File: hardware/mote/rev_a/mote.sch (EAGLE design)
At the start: 57 parts, among them Q1 CSD22206W, Q2 CSD75207W15, Q3 CSD75207W15, Q4 CSD13303W1015, Q5 CSD22206W, U1 NRF52840, U3 MAX17222, U4 TPS3839G25DBZ, U5 AB1815-T3, X1 7V-32.000MAHV-T, X2 ABS07-32.768KHZ-7-T

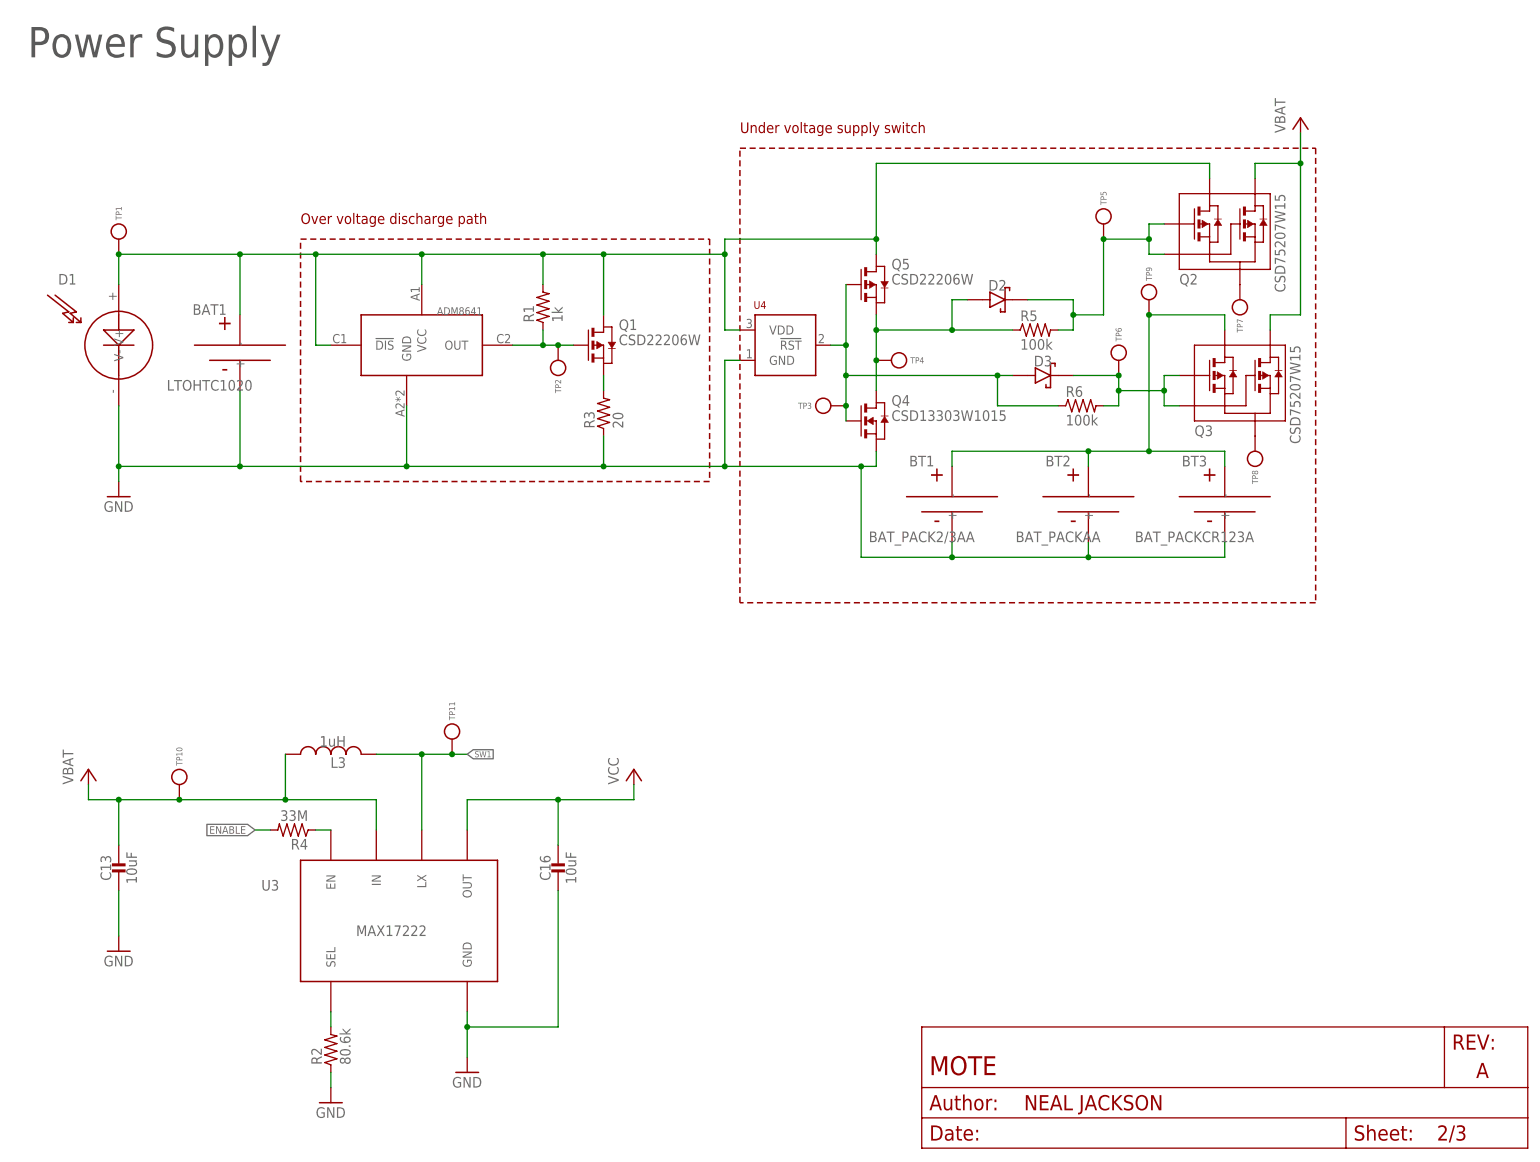
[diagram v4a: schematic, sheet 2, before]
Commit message: Schematized sensors and cleaned up
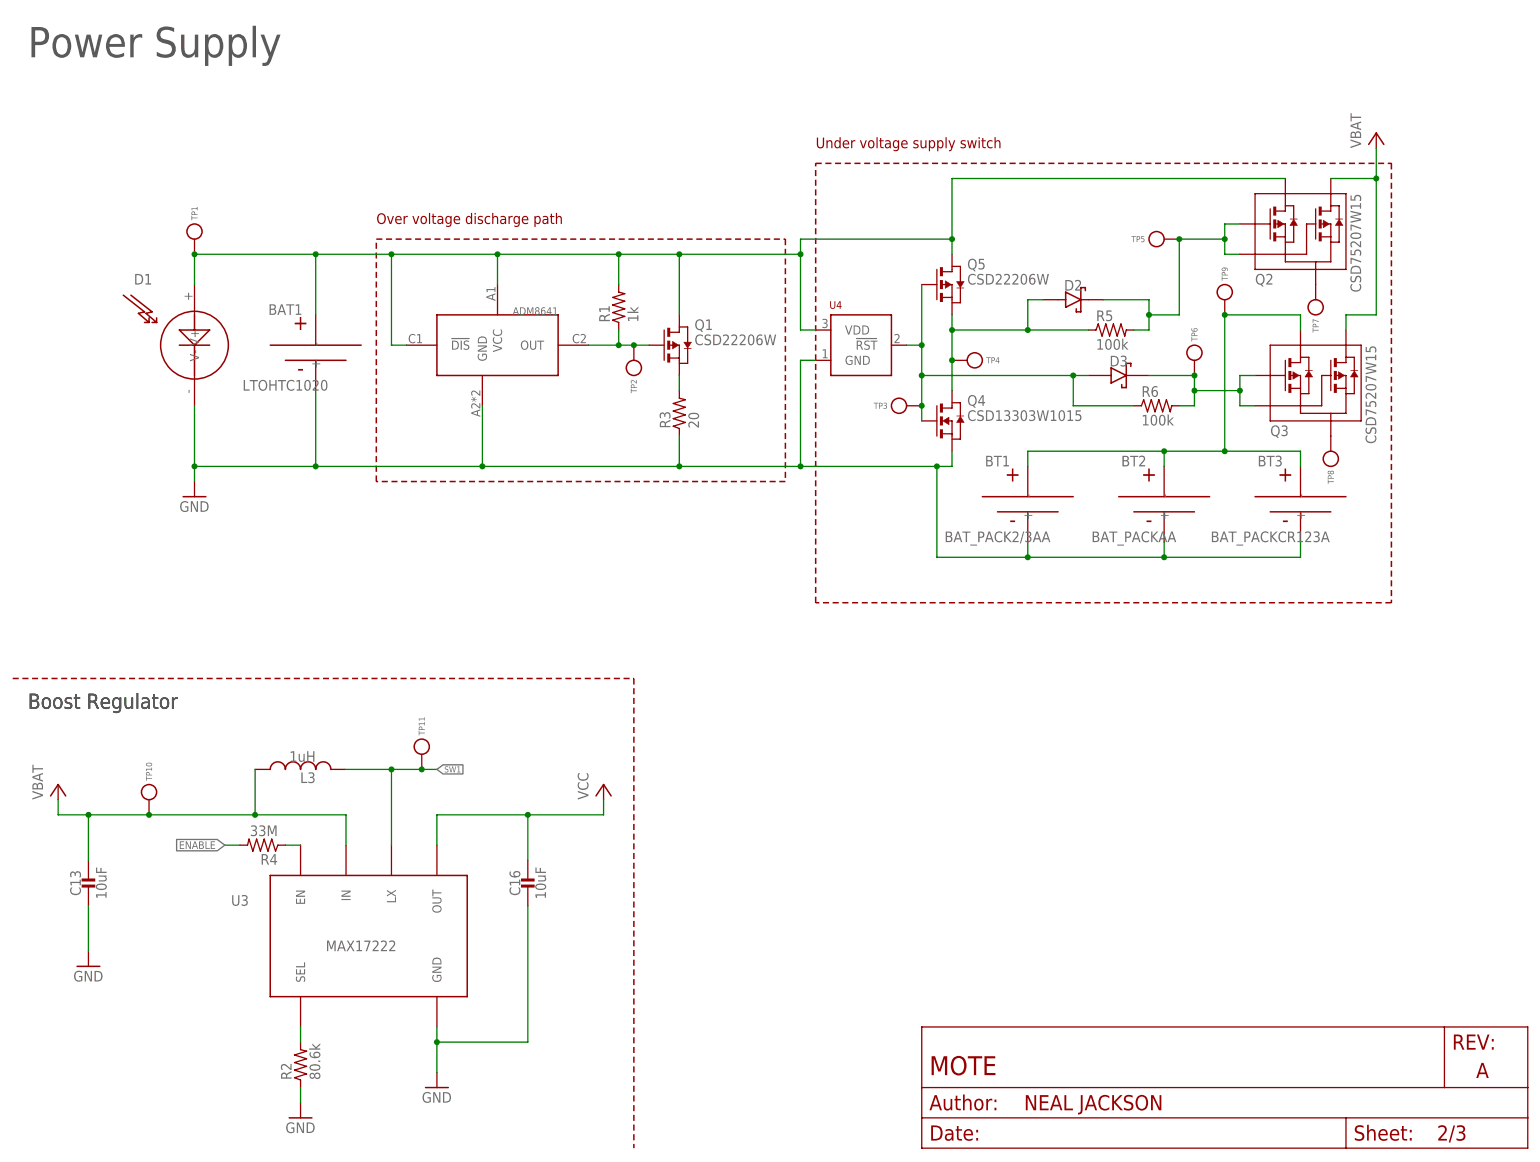
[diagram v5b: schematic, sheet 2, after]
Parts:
- removed X2: ABS07-32.768KHZ-7-T, crystals:ABS07-32.768KHZ-7-T
- added C19, C20: 0.1uF, passives:CAPACITOR0402_CAP
- added C21, C25: 1.0uF, passives:CAPACITOR0402_CAP
- added C22: 47pF, passives:CAPACITOR0402_CAP
- added C23, C24: DNP, passives:CAPACITOR0402_CAP
- added R7, R8: 10k, passives:RESISTOR0402_RES
- added U10: MS5637-02BA03, chips:MS5637-02BA03
- added U6: ISL29125, chips:ISL29125
- added U7: MAX44009, chips:MAX44009
- added U8: LIS2DW12, chips:LIS2DW12
- added U9: AB1815-T3, chips:AB1815-T3
- added X3: ABS07-32.768KHZ-7-T, crystals:ABS07-32.768KHZ-7-T
- C10: value 1uF -> 1.0uF; DIGIKEY (none) -> 490-7195-1-ND
- C17: value DNP -> 10uF; device passives:CAPACITOR0402_CAP -> passives:CAPACITOR0603_CAP; DIGIKEY (none) -> 490-3896-2-ND
- C18: value DNP -> 0.1uF; DIGIKEY (none) -> 490-6328-1-ND
- C9: value 47pF -> 0.1uF; DIGIKEY (none) -> 490-6328-1-ND
- D2, D3: value DIODE_SCHOTTKYSOD323 -> DIODE_SCHOTTKYMBR0520LT1G; device passives:DIODE_SCHOTTKYSOD323 -> passives:DIODE_SCHOTTKYMBR0520LT1G; DIGIKEY (none) -> 1727-7328-1-ND; MANUFACTURER (none) -> Nexperia; MPN (none) -> BAT54GWJ
- R1: DIGIKEY (none) -> 311-1.0KJRCT-ND
- R3: DIGIKEY (none) -> 311-20JRCT-ND
- R5, R6: DIGIKEY (none) -> 311-100KLRCT-ND
- U5: value AB1815-T3 -> SI7021-A20-GM1; device chips:AB1815-T3 -> chips:SI7021-A20-GM1
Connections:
- removed net N$19: C17.1, U5.XI, X2.1
- removed net N$20: C18.1, U5.XO, X2.2
- removed net N$21: C9.1, U5.AF
- new net !CLR_INT: U6.!INT
- new net !LGHT_INT: U7.!INT
- new net ACL_CS: U8.CS
- new net ACL_INT1: U8.INT1
- new net ACL_INT2: U8.INT2
- new net N$25: C22.1, U9.AF
- new net N$26: C23.1, U9.XI, X3.1
- new net N$27: C24.1, U9.XO, X3.2
- new net SCK: U8.SCL/SPC, U9.SCL
- new net SDA: R8.1, U10.SDA, U5.SDA, U6.SDA, U7.SDA
- net !RTC_EXTR: now also U9.!EXTR; no longer U5.!EXTR
- net !RTC_IRQ1: now also U9.FOUT/!IRQ1; no longer U5.FOUT/!IRQ1
- net !RTC_IRQ2: now also U9.!IRQ2; no longer U5.!IRQ2
- net !RTC_RESET: now also U9.!RST; no longer U5.!RST
- net CLKOUT: now also U9.CLKOUT/!IRQ3; no longer U5.CLKOUT/!IRQ3
- net CS_RTC: now also U9.!CS; no longer U5.!CS
- net GND: now also C19.2, C20.2, C21.2, C22.2, C23.2, C24.2, C25.2, U10.GND, U5.GND, U6.GND, U7.A0, U7.GND, U8.GND, U9.VSS; no longer U5.VSS
- net MISO: now also U8.MISO/SDA, U9.SDO; no longer U5.SDO
- net MOSI: now also U8.MOSI/SA0, U9.SDI; no longer U5.SDI
- net SCL: now also R7.1, U10.SCL, U6.SCL, U7.SCL
- net VCC: now also C17.1, C18.1, C19.1, C20.1, C21.1, C25.1, C9.1, R7.2, R8.2, U10.VDD, U6.VDD, U7.VCC, U8.VCC, U8.VDD_IO, U9.VCC
- net WDI: now also U9.WDI; no longer U5.WDI
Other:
- note added: "Accelerometer"
- note added: "Ambient Light"
- note added: "Boost Regulator"
- note added: "Humidity"
- note added: "Light Color"
- note added: "Pressure"
- note added: "RTC"
- note added: "Sensors"
- note added: "Temperature"
- moved on the sheet: A1, BAT1, BT1, BT2, BT3, C10, C13, C16, C17, C18, C9, D1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

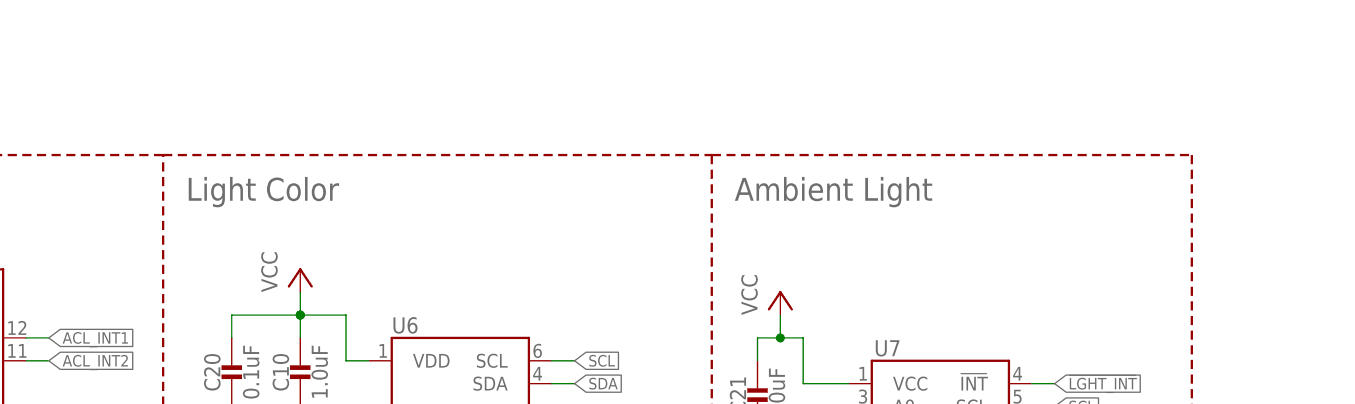
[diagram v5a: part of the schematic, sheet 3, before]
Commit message: add light subdivision
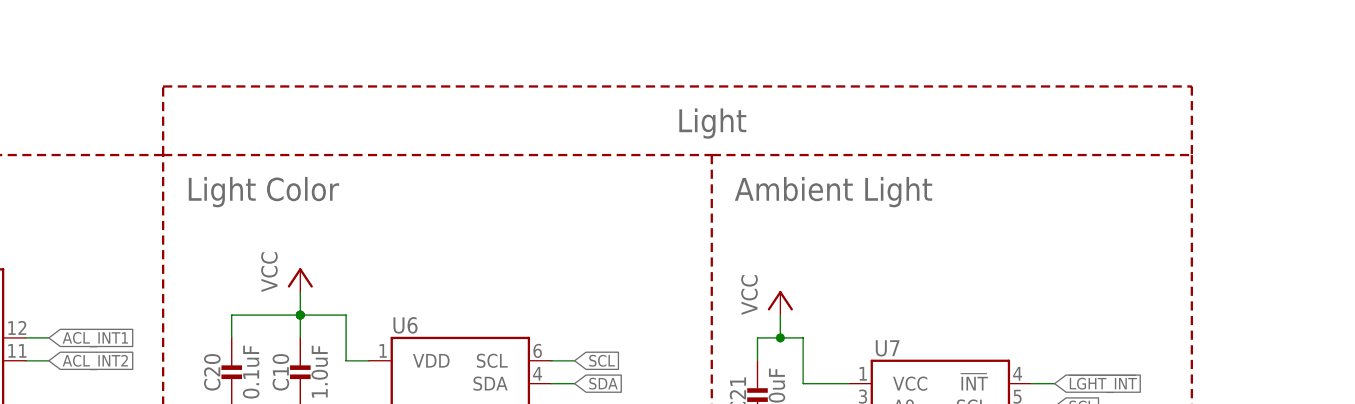
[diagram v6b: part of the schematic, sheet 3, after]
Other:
- note added: "Light"
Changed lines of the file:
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@@
 <wire x1="53.34" y1="121.92" x2="104.14" y2="121.92" width="0.254" layer="94" style="shortdash"/>
 <wire x1="53.34" y1="121.92" x2="0" y2="121.92" width="0.254" layer="94" style="shortdash"/>
+<text x="142.24" y="177.8" size="2.54" layer="95" align="bottom-center">Light</text>
+<wire x1="81.28" y1="175.26" x2="81.28" y2="182.88" width="0.254" layer="94" style="shortdash"/>
+<wire x1="81.28" y1="182.88" x2="195.58" y2="182.88" width="0.254" layer="94" style="shortdash"/>
+<wire x1="195.58" y1="182.88" x2="195.58" y2="175.26" width="0.254" layer="94" style="shortdash"/>
 </plain>
 <instances>

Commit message: made changes from josh
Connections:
- removed net !RTC_RESET: U9.!RST
- removed net N$22: BT1.+, BT2.+, BT3.+, Q3.D1, TP9.TESTPOINT
- new net !RST: U1.P0.18/RST, U9.!RST
- new net VSW: C13.1, L3.1, Q2.D2, Q3.D2, TP10.TESTPOINT, U3.IN
- net N$1: now also Q5.D; no longer Q5.S
- net N$24: now also Q5.S; no longer Q5.D
- net VBAT: now also BT1.+, BT2.+, BT3.+, C25.1, Q3.D1, TP9.TESTPOINT, U9.VCC; no longer C13.1, L3.1, Q2.D2, Q3.D2, TP10.TESTPOINT, U3.IN
- net VCC: no longer C25.1, U9.VCC
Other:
- moved on the sheet: C22, C23, C24, C25, D2, D3, Q2, Q3, Q4, Q5, R5, R6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

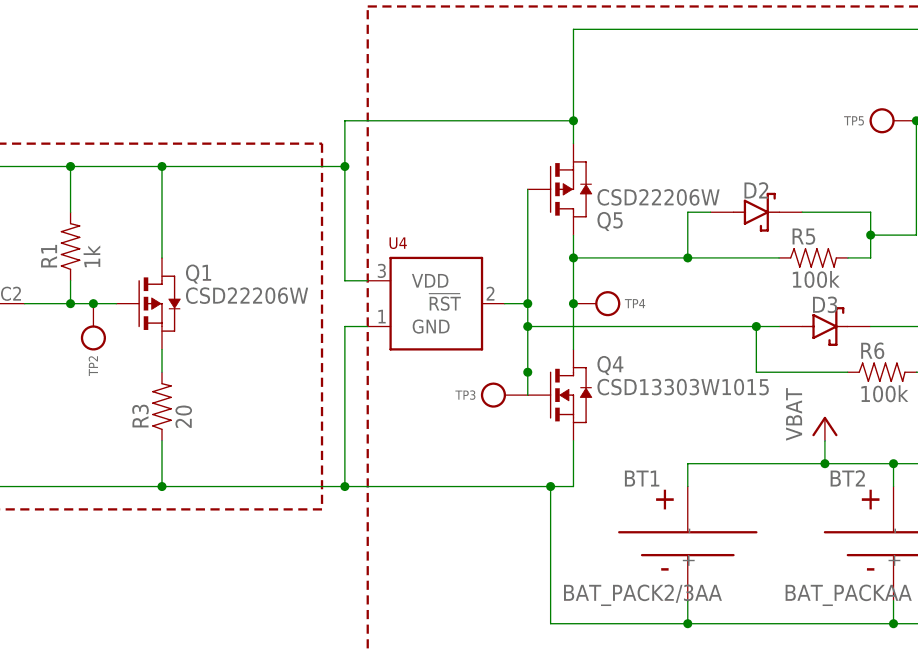
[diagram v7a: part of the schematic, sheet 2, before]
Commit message: Do undervoltage check in software
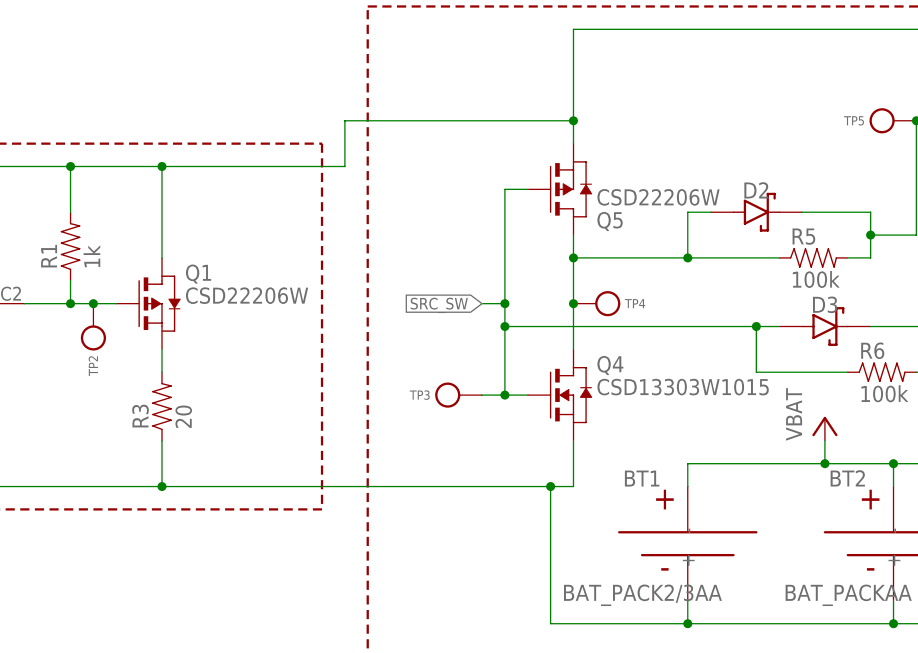
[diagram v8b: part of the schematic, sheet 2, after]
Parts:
- removed U4: TPS3839G25DBZ, chips:TPS3839G25DBZ
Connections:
- removed net N$15: D3.ANODE, Q4.G, Q5.G, R6.1, TP3.TESTPOINT, U4.!RST
- new net SRC_SW: D3.ANODE, Q4.G, Q5.G, R6.1, TP3.TESTPOINT
- net GND: no longer U4.GND
- net N$24: no longer U4.VDD
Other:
- moved on the sheet: TP3
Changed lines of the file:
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@@
 "/>
 </part>
-<part name="U4" library="chips" deviceset="TPS3839" device="G25DBZ"/>
 <part name="Q2" library="fets" deviceset="CSD75207W15" device=""/>
 <part name="Q3" library="fets" deviceset="CSD75207W15" device=""/>
@@
 <attribute name="DIGIKEY" x="111.76" y="124.46" size="1.778" layer="96" rot="R90" display="off"/>
 </instance>
-<instance part="U4" gate="G$1" x="137.16" y="129.54"/>
 <instance part="Q2" gate="G$1" x="215.9" y="157.48" rot="MR0"/>
 <instance part="Q3" gate="G$1" x="218.44" y="132.08" rot="MR0"/>
@@
 <instance part="TP1" gate="G$1" x="30.48" y="152.4" rot="R270"/>
 <instance part="TP2" gate="G$1" x="104.14" y="132.08" rot="R90"/>
-<instance part="TP3" gate="G$1" x="149.86" y="124.46"/>
+<instance part="TP3" gate="G$1" x="144.78" y="124.46"/>
 <instance part="TP4" gate="G$1" x="160.02" y="134.62" rot="R180"/>
 <instance part="TP5" gate="G$1" x="193.04" y="154.94"/>
@@
 </segment>
 <segment>
-<wire x1="111.76" y1="114.3" x2="132.08" y2="114.3" width="0.1524" layer="91"/>
-<wire x1="132.08" y1="114.3" x2="132.08" y2="132.08" width="0.1524" layer="91"/>
-<pinref part="U4" gate="G$1" pin="GND"/>
-<wire x1="132.08" y1="132.08" x2="134.62" y2="132.08" width="0.1524" layer="91"/>
 <pinref part="Q4" gate="G$1" pin="S"/>
-<wire x1="132.08" y1="114.3" x2="154.94" y2="114.3" width="0.1524" layer="91"/>
+<wire x1="111.76" y1="114.3" x2="154.94" y2="114.3" width="0.1524" layer="91"/>
 <wire x1="154.94" y1="114.3" x2="157.48" y2="114.3" width="0.1524" layer="91"/>
 <wire x1="157.48" y1="114.3" x2="157.48" y2="119.38" width="0.1524" layer="91"/>
-<junction x="132.08" y="114.3"/>
 <pinref part="R3" gate="G$1" pin="1"/>
 <wire x1="111.76" y1="119.38" x2="111.76" y2="114.3" width="0.1524" layer="91"/>
@@
 </segment>
 </net>
-<net name="N$15" class="0">
+<net name="SRC_SW" class="0">
 <segment>
 <wire x1="177.8" y1="132.08" x2="180.34" y2="132.08" width="0.1524" layer="91"/>
 <wire x1="177.8" y1="132.08" x2="177.8" y2="127" width="0.1524" layer="91"/>
 <wire x1="177.8" y1="127" x2="187.96" y2="127" width="0.1524" layer="91"/>
-<pinref part="U4" gate="G$1" pin="!RST"/>
-<wire x1="149.86" y1="134.62" x2="152.4" y2="134.62" width="0.1524" layer="91"/>
 <pinref part="Q5" gate="G$1" pin="G"/>
-<pinref part="Q4" gate="G$1" pin="G"/>
-<wire x1="152.4" y1="134.62" x2="152.4" y2="147.32" width="0.1524" layer="91"/>
-<wire x1="152.4" y1="134.62" x2="152.4" y2="132.08" width="0.1524" layer="91"/>
-<junction x="152.4" y="134.62"/>
-<wire x1="152.4" y1="132.08" x2="152.4" y2="124.46" width="0.1524" layer="91"/>
-<wire x1="177.8" y1="132.08" x2="152.4" y2="132.08" width="0.1524" layer="91"/>
+<wire x1="149.86" y1="134.62" x2="149.86" y2="147.32" width="0.1524" layer="91"/>
+<wire x1="149.86" y1="147.32" x2="152.4" y2="147.32" width="0.1524" layer="91"/>
+<wire x1="149.86" y1="134.62" x2="149.86" y2="132.08" width="0.1524" layer="91"/>
+<junction x="149.86" y="134.62"/>
+<wire x1="177.8" y1="132.08" x2="149.86" y2="132.08" width="0.1524" layer="91"/>
 <junction x="177.8" y="132.08"/>
-<junction x="152.4" y="132.08"/>
-<pinref part="TP3" gate="G$1" pin="TESTPOINT"/>
-<junction x="152.4" y="127"/>
 <pinref part="R6" gate="G$1" pin="1"/>
 <pinref part="D3" gate="G$1" pin="ANODE"/>
+<wire x1="149.86" y1="134.62" x2="147.32" y2="134.62" width="0.1524" layer="91"/>
+<pinref part="Q4" gate="G$1" pin="G"/>
+<pinref part="TP3" gate="G$1" pin="TESTPOINT"/>
+<wire x1="147.32" y1="124.46" x2="149.86" y2="124.46" width="0.1524" layer="91"/>
+<wire x1="149.86" y1="124.46" x2="152.4" y2="124.46" width="0.1524" layer="91"/>
+<wire x1="149.86" y1="132.08" x2="149.86" y2="124.46" width="0.1524" layer="91"/>
+<junction x="149.86" y="132.08"/>
+<junction x="149.86" y="124.46"/>
+<label x="147.32" y="134.62" size="1.27" layer="95" rot="R180" xref="yes"/>
 </segment>
 </net>
@@
 <wire x1="111.76" y1="149.86" x2="101.6" y2="149.86" width="0.1524" layer="91"/>
 <junction x="101.6" y="149.86"/>
-<pinref part="U4" gate="G$1" pin="VDD"/>
-<wire x1="134.62" y1="137.16" x2="132.08" y2="137.16" width="0.1524" layer="91"/>
-<wire x1="132.08" y1="137.16" x2="132.08" y2="149.86" width="0.1524" layer="91"/>
 <wire x1="132.08" y1="149.86" x2="111.76" y2="149.86" width="0.1524" layer="91"/>
 <junction x="111.76" y="149.86"/>
 <wire x1="132.08" y1="154.94" x2="132.08" y2="149.86" width="0.1524" layer="91"/>
-<junction x="132.08" y="149.86"/>
 <pinref part="TP1" gate="G$1" pin="TESTPOINT"/>
 <junction x="30.48" y="149.86"/>
